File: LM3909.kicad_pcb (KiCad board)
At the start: 2 copper layers, 16 parts, among them Q1 2N3904, Q2A1 2N3906, Q2B1 2N3906, Q3 2N3904, Q4 2N3904

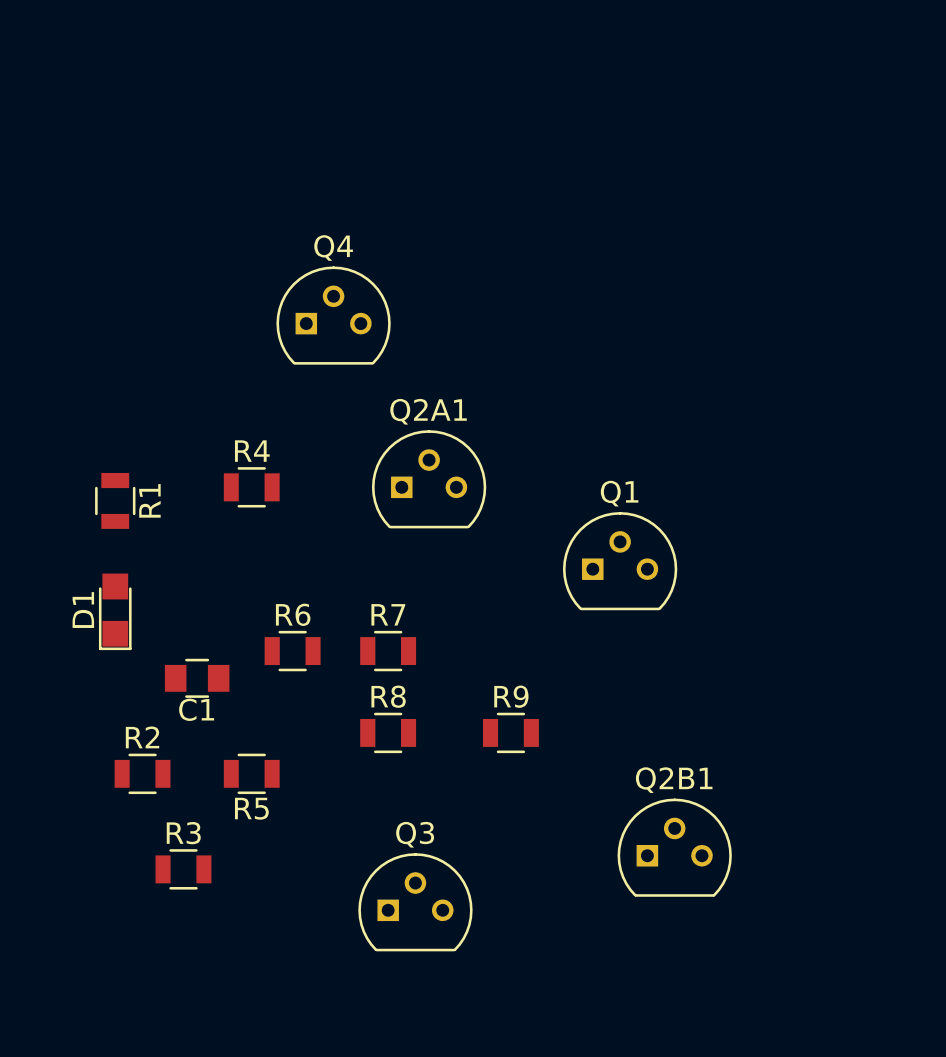
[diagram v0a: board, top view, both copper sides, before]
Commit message: start to lay traces
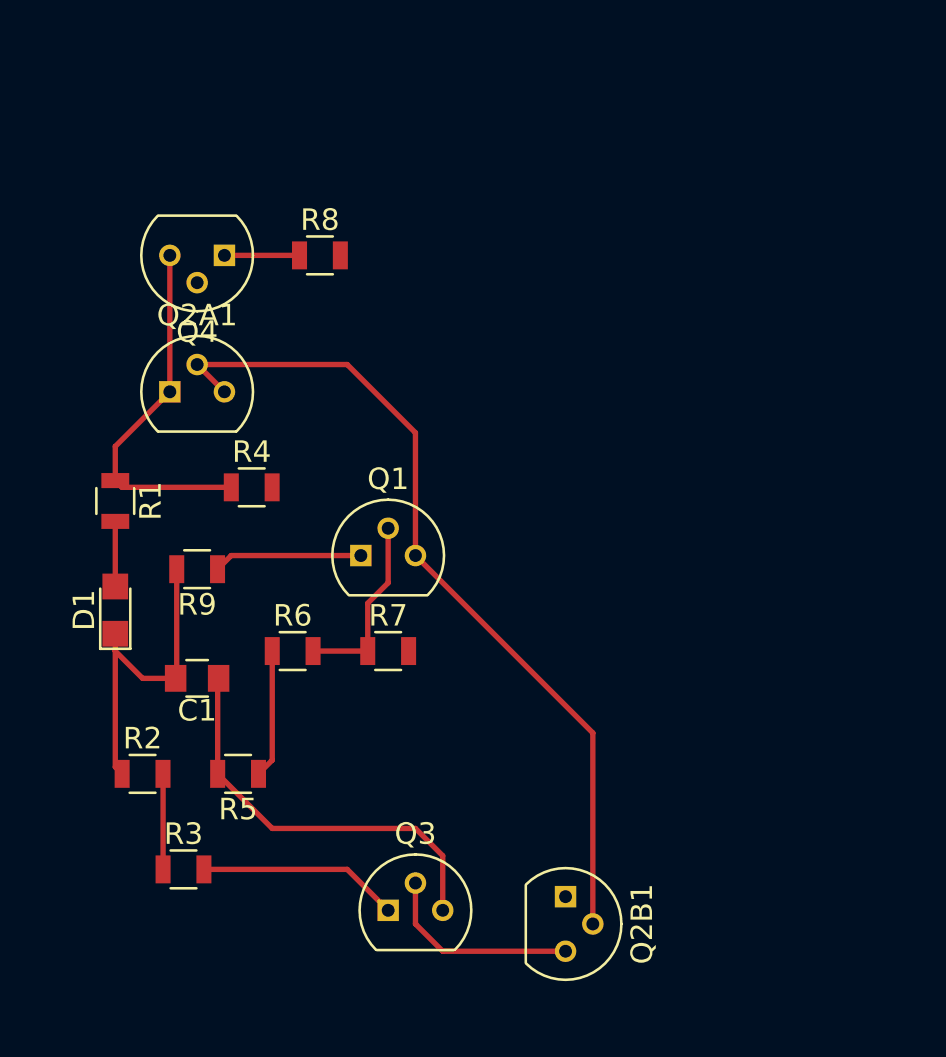
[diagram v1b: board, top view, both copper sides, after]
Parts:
- moved R8 22.5 mm to (132.1, 92.7)
- moved R9 16.5 mm to (126.4, 107.3), turned to 180 degrees
- moved Q2A1 11.7 mm to (125.1, 99.1)
- moved Q1 10.8 mm to (134.0, 106.7)
- moved Q4 4.96 mm to (127.6, 92.7), turned to 180 degrees
- moved Q2B1 4.26 mm to (143.5, 122.6), turned to 270 degrees
- moved R5 0.63 mm to (128.3, 116.8)
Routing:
- net Net-(Q1-Pad3): track 0.00 -> 39.6 mm
- net Net-(C1-Pad1): track 0.00 -> 19.1 mm
- net Net-(BT1-Pad1): track 0.00 -> 17.1 mm
- net Net-(C1-Pad2): track 0.00 -> 15.1 mm
- net Net-(Q2B1-Pad3): track 0.00 -> 9.42 mm
- net Net-(BT1-Pad2): track 0.00 -> 9.36 mm
- net Net-(Q1-Pad2): track 0.00 -> 8.65 mm
- net Net-(Q1-Pad1): track 0.00 -> 6.93 mm
- net Net-(Q4-Pad2): track 0.00 -> 5.98 mm
- net Net-(R2-Pad2): track 0.00 -> 4.45 mm
- net Net-(Q4-Pad1): track 0.00 -> 3.49 mm
- net Net-(D1-Pad2): track 0.00 -> 3.03 mm

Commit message: replace through hole transistors with smd parts
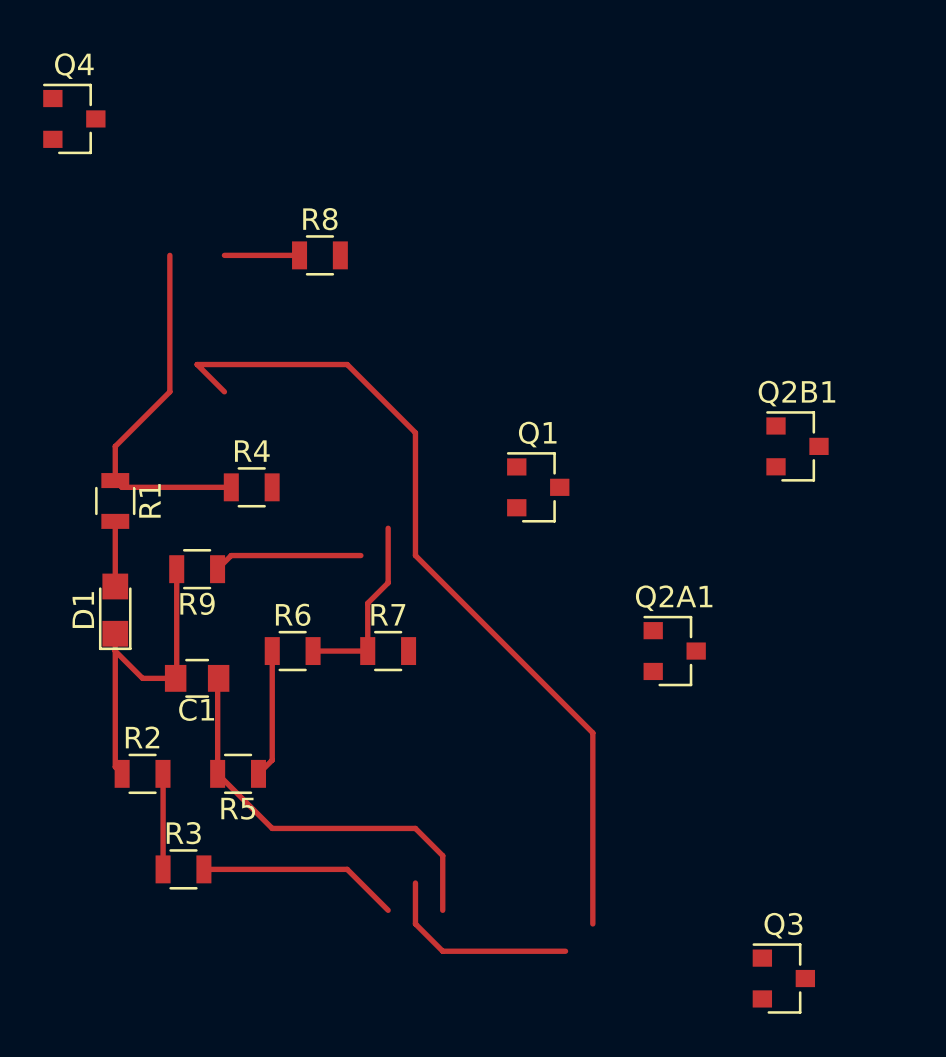
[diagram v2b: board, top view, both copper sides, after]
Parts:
- Q1, Q3, Q4: value 2N3904 -> BC847; footprint TO_SOT_Packages_THT:TO-92_Molded_Narrow -> TO_SOT_Packages_SMD:SOT-23
- Q2A1, Q2B1: value 2N3906 -> BC807; footprint TO_SOT_Packages_THT:TO-92_Molded_Narrow -> TO_SOT_Packages_SMD:SOT-23
- moved Q2A1 26.4 mm to (148.6, 111.1)
- moved Q2B1 23.6 mm to (154.3, 101.6), turned to 0 degrees
- moved Q3 18.7 mm to (153.7, 126.4)
- moved Q4 9.44 mm to (120.7, 86.4), turned to 0 degrees
- moved Q1 8.84 mm to (142.2, 103.5)
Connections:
- Q2A1 pad 1: Net-(BT1-Pad1) -> Net-(Q1-Pad3)
- Q2A1 pad 2: Net-(Q1-Pad3) -> Net-(BT1-Pad1)
- Q2B1 pad 1: Net-(BT1-Pad1) -> Net-(Q1-Pad3)
- Q2B1 pad 2: Net-(Q1-Pad3) -> Net-(BT1-Pad1)
- Q3 pad 1: Net-(BT1-Pad2) -> Net-(Q2B1-Pad3)
- Q3 pad 2: Net-(Q2B1-Pad3) -> Net-(BT1-Pad2)
- R4 pad 2: Net-(Q4-Pad2) -> Net-(Q4-Pad1)
- R5 pad 1: Net-(Q4-Pad2) -> Net-(Q4-Pad1)
- R6 pad 1: Net-(Q4-Pad2) -> Net-(Q4-Pad1)
- R6 pad 2: Net-(Q1-Pad2) -> Net-(Q1-Pad1)
- R7 pad 1: Net-(Q1-Pad2) -> Net-(Q1-Pad1)
- R7 pad 2: Net-(Q4-Pad1) -> Net-(Q4-Pad2)
- R8 pad 1: Net-(Q4-Pad1) -> Net-(Q4-Pad2)
- R9 pad 1: Net-(Q1-Pad1) -> Net-(Q1-Pad2)
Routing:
- net (no net): track 0.00 -> 49.0 mm
- net Net-(Q1-Pad3): track 39.6 -> 0.00 mm
- net Net-(Q2B1-Pad3): track 9.42 -> 0.00 mm
- net Net-(Q4-Pad2): track 5.98 -> 3.49 mm
- net Net-(Q4-Pad1): track 3.49 -> 5.98 mm
- net Net-(Q1-Pad2): track 8.65 -> 6.93 mm
- net Net-(Q1-Pad1): track 6.93 -> 8.65 mm

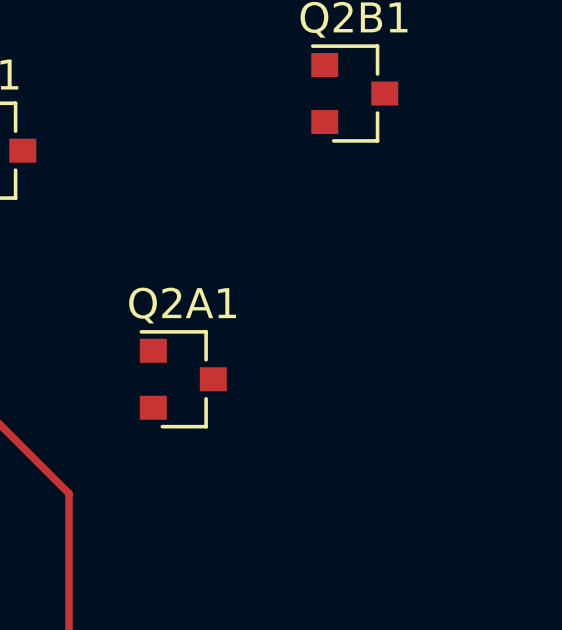
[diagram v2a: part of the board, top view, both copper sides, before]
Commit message: add another R that can be used intead of transistor current mirror
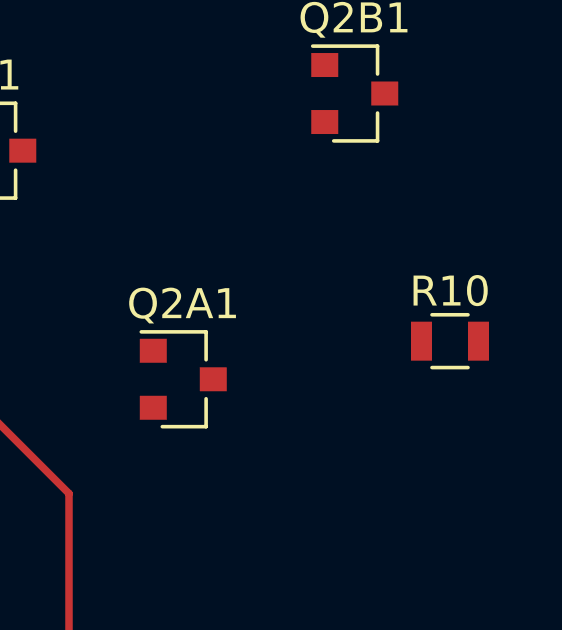
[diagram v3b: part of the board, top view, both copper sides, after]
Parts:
- added R10: 0, Resistors_SMD:R_0805, F.Cu at (157.5, 109.9)
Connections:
- Q3 pad 1: Net-(Q2B1-Pad3) -> Net-(Q3-Pad1)
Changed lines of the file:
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@@
 (kicad_pcb (version 4) (host pcbnew 4.0.7)
   (general
-    (links 25)
-    (no_connects 16)
+    (links 26)
+    (no_connects 17)
     (area 0 0 0 0)
     (thickness 1.6)
@@
     (tracks 41)
     (zones 0)
-    (modules 16)
-    (nets 13)
+    (modules 17)
+    (nets 14)
   )
   (page A4)
@@
   (net 11 "Net-(Q4-Pad1)")
   (net 12 "Net-(R2-Pad2)")
+  (net 13 "Net-(Q3-Pad1)")
   (net_class Default "This is the default net class."
     (clearance 0.2)
@@
     (add_net "Net-(Q1-Pad3)")
     (add_net "Net-(Q2B1-Pad3)")
+    (add_net "Net-(Q3-Pad1)")
     (add_net "Net-(Q4-Pad1)")
     (add_net "Net-(Q4-Pad2)")
@@
     (fp_line (start 0.76 1.58) (end -0.7 1.58) (layer F.SilkS) (width 0.12))
     (pad 1 smd rect (at -1 -0.95) (size 0.9 0.8) (layers F.Cu F.Paste F.Mask)
-      (net 8 "Net-(Q2B1-Pad3)"))
+      (net 13 "Net-(Q3-Pad1)"))
     (pad 2 smd rect (at -1 0.95) (size 0.9 0.8) (layers F.Cu F.Paste F.Mask)
       (net 9 "Net-(BT1-Pad2)"))
@@
       (at (xyz 0 0 0))
       (scale (xyz 1 1 1))
+      (rotate (xyz 0 0 0))
+    )
+  )
+  (module Resistors_SMD:R_0805 (layer F.Cu)
+    (at 157.48 109.855)
+    (descr "Resistor SMD 0805, reflow soldering, Vishay (see dcrcw.pdf)")
+    (tags "resistor 0805")
+    (attr smd)
+    (fp_text reference R10 (at 0 -1.65) (layer F.SilkS)
+      (effects (font (size 1 1) (thickness 0.15)))
+    )
+    (fp_text value 0 (at 0 1.75) (layer F.Fab)
+      (effects (font (size 1 1) (thickness 0.15)))
+    )
+    (fp_text user %R (at 0 0) (layer F.Fab)
+      (effects (font (size 0.5 0.5) (thickness 0.075)))
+    )
+    (fp_line (start -1 0.62) (end -1 -0.62) (layer F.Fab) (width 0.1))
+    (fp_line (start 1 0.62) (end -1 0.62) (layer F.Fab) (width 0.1))
+    (fp_line (start 1 -0.62) (end 1 0.62) (layer F.Fab) (width 0.1))
+    (fp_line (start -1 -0.62) (end 1 -0.62) (layer F.Fab) (width 0.1))
+    (fp_line (start 0.6 0.88) (end -0.6 0.88) (layer F.SilkS) (width 0.12))
+    (fp_line (start -0.6 -0.88) (end 0.6 -0.88) (layer F.SilkS) (width 0.12))
+    (fp_line (start -1.55 -0.9) (end 1.55 -0.9) (layer F.CrtYd) (width 0.05))
+    (fp_line (start -1.55 -0.9) (end -1.55 0.9) (layer F.CrtYd) (width 0.05))
+    (fp_line (start 1.55 0.9) (end 1.55 -0.9) (layer F.CrtYd) (width 0.05))
+    (fp_line (start 1.55 0.9) (end -1.55 0.9) (layer F.CrtYd) (width 0.05))
+    (pad 1 smd rect (at -0.95 0) (size 0.7 1.3) (layers F.Cu F.Paste F.Mask)
+      (net 8 "Net-(Q2B1-Pad3)"))
+    (pad 2 smd rect (at 0.95 0) (size 0.7 1.3) (layers F.Cu F.Paste F.Mask)
+      (net 13 "Net-(Q3-Pad1)"))
+    (model ${KISYS3DMOD}/Resistors_SMD.3dshapes/R_0805.wrl
+      (at (xyz 0 0 0))
+      (scale (xyz 1 1 1))

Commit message: route some more
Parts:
- moved Q3 29.3 mm to (131.4, 107.3), turned to 180 degrees
- moved Q2B1 23.3 mm to (137.8, 118.1)
- moved Q2A1 17.3 mm to (132.7, 118.1)
- moved R10 13.9 mm to (144.8, 115.6)
- moved Q4 13.1 mm to (125.7, 98.4), turned to 180 degrees
- moved Q1 8.35 mm to (141.0, 111.8), turned to 270 degrees
- moved R8 4.49 mm to (131.4, 97.2)
- turned R3 to 270 degrees
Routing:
- net (no net): track 49.0 -> 0.00 mm
- net Net-(BT1-Pad2): track 9.36 -> 56.6 mm
- net Net-(BT1-Pad1): track 17.1 -> 47.7 mm
- net Net-(Q3-Pad1): track 0.00 -> 19.8 mm
- net Net-(Q1-Pad3): track 0.00 -> 12.0 mm
- net Net-(C1-Pad1): track 19.1 -> 10.8 mm
- net Net-(Q1-Pad2): track 6.93 -> 0.00 mm
- net Net-(Q1-Pad1): track 8.65 -> 14.8 mm
- net Net-(Q2B1-Pad3): track 0.00 -> 6.09 mm
- net Net-(Q4-Pad1): track 5.98 -> 11.4 mm
- net Net-(R2-Pad2): track 4.45 -> 3.90 mm

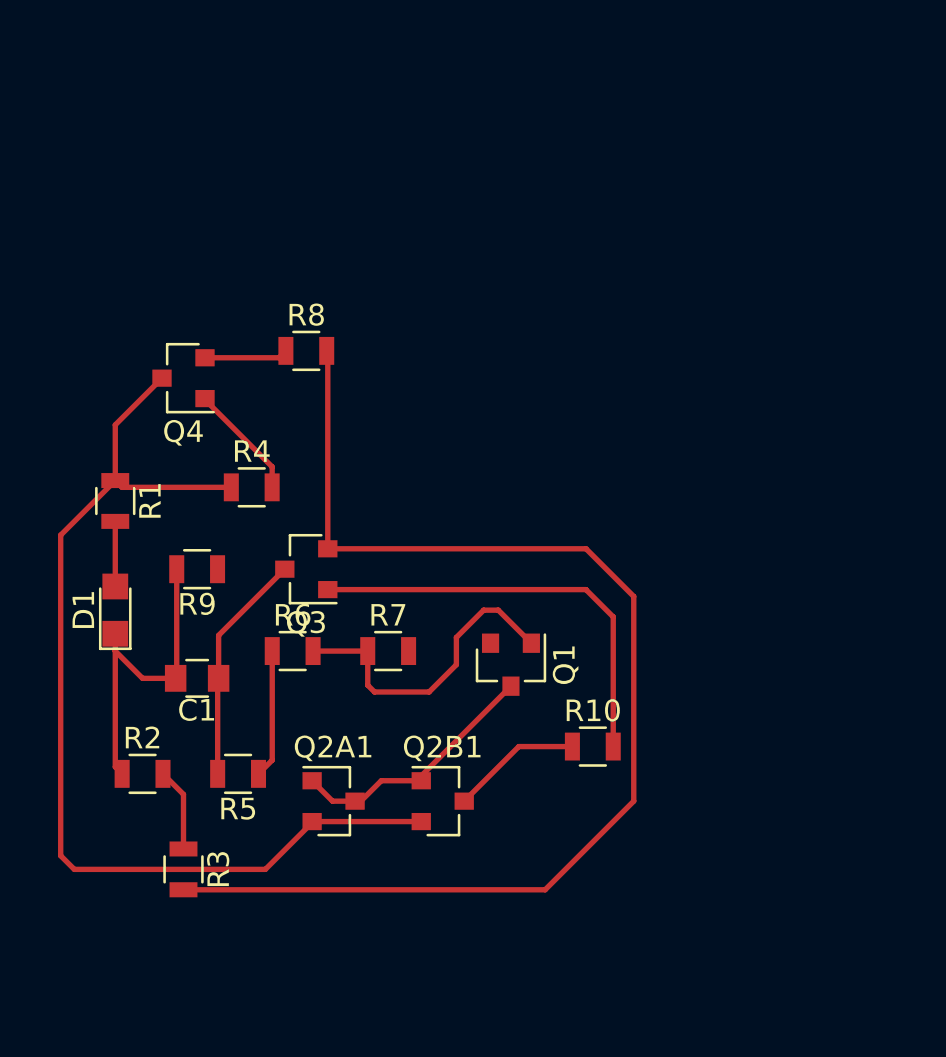
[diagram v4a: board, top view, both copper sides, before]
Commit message: connected everything on one layer
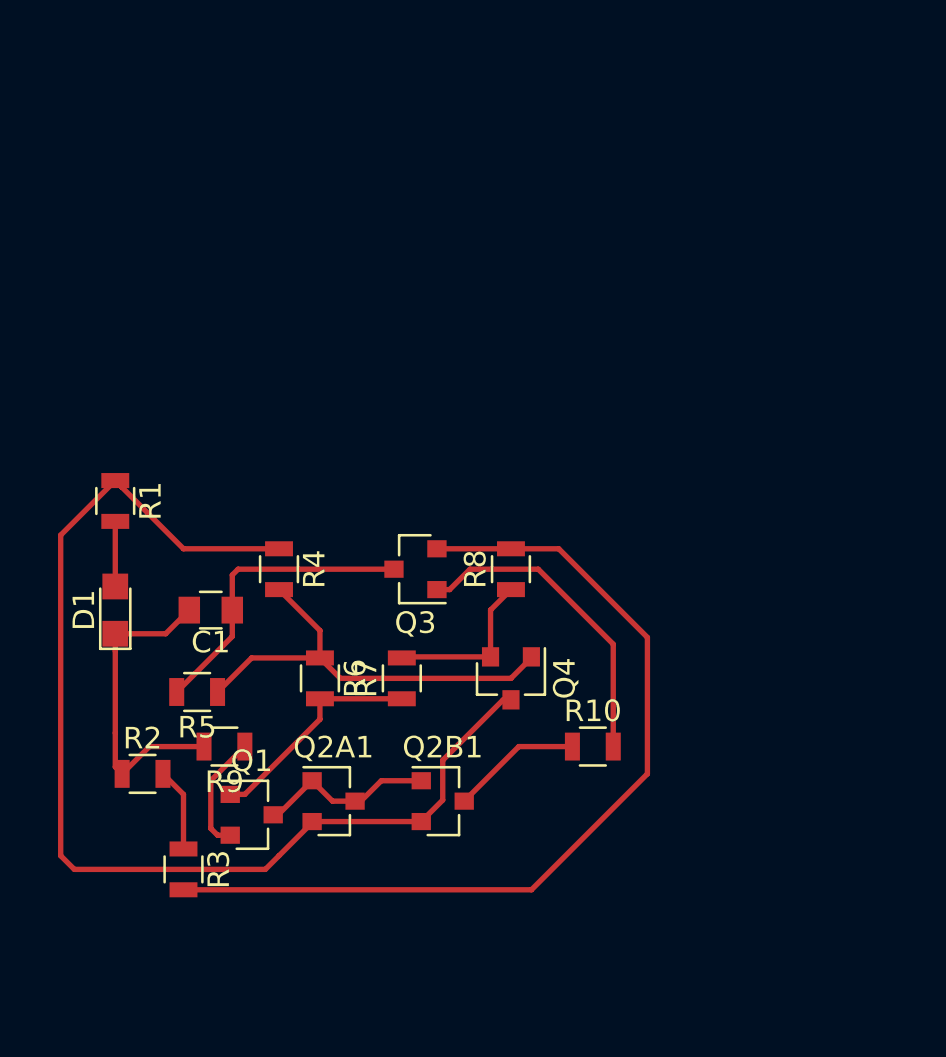
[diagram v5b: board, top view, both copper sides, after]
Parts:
- moved Q4 20.7 mm to (141.0, 112.4), turned to 270 degrees
- moved Q1 13.9 mm to (128.9, 118.7), turned to 0 degrees
- moved R8 13.9 mm to (141.0, 107.3), turned to 90 degrees
- moved R9 8.35 mm to (127.6, 115.6)
- moved Q3 5.08 mm to (136.5, 107.3)
- moved R5 4.26 mm to (126.4, 113.0)
- moved R4 4.02 mm to (130.2, 107.3), turned to 270 degrees
- moved C1 3.24 mm to (127.0, 109.2)
- moved R6 1.80 mm to (132.1, 112.4), turned to 270 degrees
- moved R7 1.42 mm to (135.9, 112.4), turned to 90 degrees
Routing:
- net Net-(BT1-Pad2): track 56.6 -> 41.7 mm
- net Net-(Q4-Pad1): track 11.4 -> 20.1 mm
- net Net-(BT1-Pad1): track 47.7 -> 53.5 mm
- net Net-(Q1-Pad2): track 0.00 -> 5.50 mm
- net Net-(Q3-Pad1): track 19.8 -> 14.8 mm
- net Net-(Q1-Pad1): track 14.8 -> 10.4 mm
- net Net-(Q4-Pad2): track 3.90 -> 7.67 mm
- net Net-(Q1-Pad3): track 12.0 -> 8.56 mm
- net Net-(C1-Pad1): track 10.8 -> 14.2 mm

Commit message: condensed
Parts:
- moved C1 3.42 mm to (125.7, 112.4), turned to 270 degrees
- moved D1 3.17 mm to (122.6, 112.4)
- moved R1 3.17 mm to (122.6, 107.3)
- moved R5 2.84 mm to (128.9, 111.8)
- moved R10 2.84 mm to (142.2, 116.8), turned to 90 degrees
- moved R9 2.69 mm to (125.7, 117.5), turned to 90 degrees
- moved R2 1.80 mm to (122.6, 118.1), turned to 270 degrees
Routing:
- net Net-(C1-Pad2): track 14.9 -> 6.67 mm
- net Net-(BT1-Pad1): track 53.5 -> 48.4 mm
- net Net-(Q4-Pad1): track 20.1 -> 17.0 mm
- net Net-(C1-Pad1): track 14.2 -> 17.0 mm
- net Net-(Q1-Pad2): track 5.50 -> 2.70 mm
- net Net-(Q2B1-Pad3): track 6.09 -> 3.58 mm
- net Net-(BT1-Pad2): track 41.7 -> 39.6 mm

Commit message: much smaller
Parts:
- moved Q4 3.70 mm to (137.8, 114.3)
- moved R8 3.70 mm to (139.1, 110.5)
- moved R10 2.84 mm to (139.7, 118.1)
- moved R3 2.84 mm to (123.2, 120.0)
- moved R4 2.62 mm to (129.5, 109.9)
- moved R7 2.29 mm to (134.6, 114.3)
- moved Q3 2.01 mm to (135.9, 109.2)
- moved R2 2.01 mm to (123.2, 116.2)
- moved Q1 1.91 mm to (128.9, 116.8)
- moved R6 1.91 mm to (132.1, 114.3)
- moved Q2B1 1.80 mm to (136.5, 119.4)
- moved R1 1.42 mm to (123.2, 108.6)
- moved R5 1.27 mm to (128.9, 113.0)
- moved D1 0.63 mm to (123.2, 112.4)
- moved R9 0.63 mm to (125.7, 116.8)
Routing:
- net Net-(BT1-Pad1): track 48.4 -> 42.9 mm
- net Net-(Q4-Pad1): track 17.0 -> 12.2 mm
- net Net-(Q3-Pad1): track 14.7 -> 10.1 mm
- net Net-(C1-Pad1): track 17.0 -> 12.7 mm
- net Net-(Q1-Pad1): track 10.4 -> 6.98 mm
- net Net-(BT1-Pad2): track 39.6 -> 36.7 mm
- net Net-(Q4-Pad2): track 7.67 -> 5.24 mm
- net Net-(Q1-Pad3): track 8.56 -> 6.55 mm
- net Net-(R2-Pad2): track 3.70 -> 1.91 mm
- net Net-(Q2B1-Pad3): track 3.58 -> 2.31 mm
- net Net-(D1-Pad2): track 3.03 -> 1.76 mm
- net Net-(Q1-Pad2): track 2.70 -> 2.17 mm

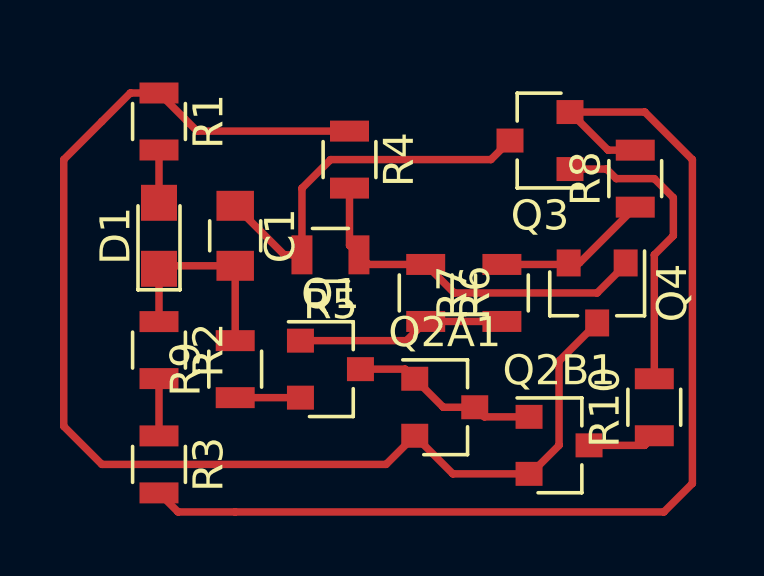
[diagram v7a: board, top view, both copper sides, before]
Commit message: loop wires other way
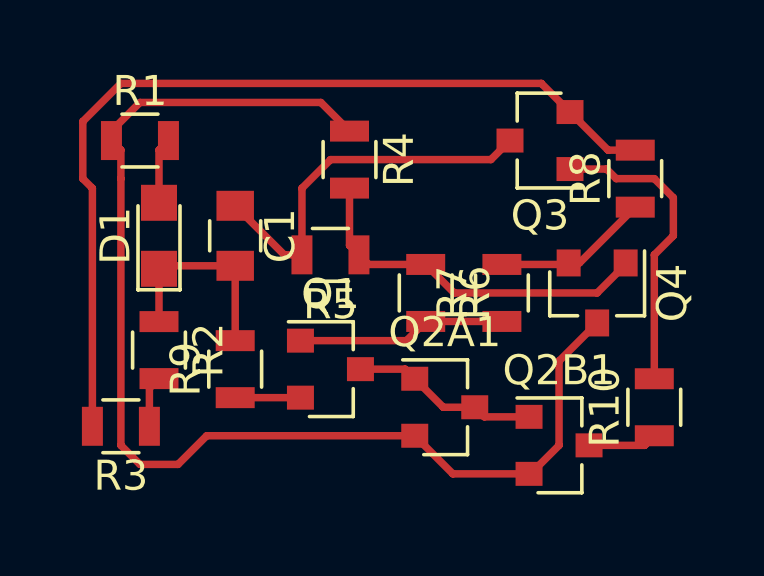
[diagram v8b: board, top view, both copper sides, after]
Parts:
- moved R3 1.80 mm to (121.9, 118.7), turned to 180 degrees
- moved R1 0.90 mm to (122.6, 109.2), turned to 0 degrees
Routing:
- net Net-(BT1-Pad2): track 36.7 -> 30.2 mm
- net Net-(BT1-Pad1): track 42.9 -> 40.2 mm
